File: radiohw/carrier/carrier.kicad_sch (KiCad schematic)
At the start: 4 parts, among them J2 Bus_M.2_Socket_B, J3 Bus_M.2_Socket_E, J5 USB_C_Receptacle, J6 USB3_A_Stacked

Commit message: Update schematics.
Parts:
- removed J2: Bus_M.2_Socket_B, symbol Connector:Bus_M.2_Socket_B
- added J4: Bus_M.2_Socket_M, symbol Connector:Bus_M.2_Socket_M
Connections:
- new net: J4.1 (GND), J4.15 (GND), J4.21 (GND), J4.27 (GND), J4.3 (GND), J4.33 (GND), J4.39 (GND), J4.45 (GND), J4.51 (GND), J4.57 (GND), J4.71 (GND), J4.73 (GND), J4.75 (GND), J4.9 (GND)
- new net: J4.12 (3.3V), J4.14 (3.3V), J4.16 (3.3V), J4.18 (3.3V), J4.2 (3.3V), J4.4 (3.3V), J4.70 (3.3V), J4.72 (3.3V), J4.74 (3.3V)
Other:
- added sheet 4GCard (4g_addon.kicad_sch)
- added sheet audio (audio.kicad_sch)
- moved on the sheet: J5, J6A, J6B
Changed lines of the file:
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@@
     (stroke (width 0) (type default))
   )
-  (symbol (lib_id "Connector:USB3_A_Stacked") (at 66.04 38.1 0) (unit 2)
-    (in_bom yes) (on_board yes) (dnp no) (fields_autoplaced)
-    (property "Reference" "J6" (at 66.04 19.05 0)
-      (effects (font (size 1.27 1.27)))
-    )
-    (property "Value" "USB3_A_Stacked" (at 66.04 21.59 0)
-      (effects (font (size 1.27 1.27)))
-    )
-    (property "Footprint" "" (at 69.85 35.56 0)
-      (effects (font (size 1.27 1.27)) hide)
-    )
-    (property "Datasheet" "~" (at 69.85 35.56 0)
+  (text_box "HDMI output\n\nAUDIO\n + 8 output channels minimum for main audio\n + 2 channel input for am/fm radio\n + 1 channel output for external radio\n + 1 channel input for external radio\n\nM2.B card for 4g addon\nM2.E card for wifi/bluetooth\nM2.M card for storage\n\nusb2\n + I touchscreen\n + I other stuff\n + E user charge only\n + E user charge only\n + E user charge only\n\nusb-c\n + user interface\n\nusb-3\n + user interface\n\ngpio\n + O winch in\n + O winch out\n + O4 window up\n + O4 window down\n + O door lock\n + O door unlock\n + O external radio trigger\n + O general led indicator\n + O fingerprint enable\n + O inverter enable\n + O4 light(s) control\n + O4 aux outputs\n + I potentiometer A for volume (quadrature)\n + I potentiometer B for volume (quadrature)\n + I potentiometer A for adjust (quadrature)\n + I potentiometer B for adjust (quadrature)\n + I button A\n + I button B\n + I fingerprint IRQ\n + I4 aux inputs\n\nuart\n + fingerprint sensor (3.3v)\n + GPS sensor\n\npcie\n + cameras add-on (on board)\n\n1G ethernet port\n\nNFC - ?\n\nam/fm radio control - ?\nam/fm radio data - ?\n\nsystem fan control and tachometer\n\nsim card connector ?"
+    (at 223.52 13.97 0) (size 55.88 149.86)
+    (stroke (width 0) (type default))
+    (fill (type none))
+    (effects (font (size 1.27 1.27)) (justify left top))
+  )
+  (symbol (lib_id "Connector:USB3_A_Stacked") (at 143.51 161.29 0) (unit 2)
+    (in_bom yes) (on_board yes) (dnp no) (fields_autoplaced)
+    (property "Reference" "J6" (at 143.51 142.24 0)
+      (effects (font (size 1.27 1.27)))
+    )
+    (property "Value" "USB3_A_Stacked" (at 143.51 144.78 0)
+      (effects (font (size 1.27 1.27)))
+    )
+    (property "Footprint" "" (at 147.32 158.75 0)
+      (effects (font (size 1.27 1.27)) hide)
+    )
+    (property "Datasheet" "~" (at 147.32 158.75 0)
       (effects (font (size 1.27 1.27)) hide)
     )
@@
     )
   )
-  (symbol (lib_id "Connector:Bus_M.2_Socket_B") (at 119.38 71.12 0) (unit 1)
-    (in_bom yes) (on_board yes) (dnp no) (fields_autoplaced)
-    (property "Reference" "J2" (at 121.5741 20.32 0)
-      (effects (font (size 1.27 1.27)) (justify left))
-    )
-    (property "Value" "Bus_M.2_Socket_B" (at 121.5741 22.86 0)
-      (effects (font (size 1.27 1.27)) (justify left))
-    )
-    (property "Footprint" "" (at 119.38 44.45 0)
-      (effects (font (size 1.27 1.27)) hide)
-    )
-    (property "Datasheet" "http://read.pudn.com/downloads794/doc/project/3133918/PCIe_M.2_Electromechanical_Spec_Rev1.0_Final_11012013_RS_Clean.pdf#page=154" (at 119.38 44.45 0)
-      (effects (font (size 1.27 1.27)) hide)
-    )
-    (pin "58")
-    (pin "4")
-    (pin "61")
-    (pin "44")
-    (pin "39")
-    (pin "59")
-    (pin "62")
-    (pin "60")
-    (pin "63")
-    (pin "25")
-    (pin "24")
-    (pin "26")
-    (pin "5")
-    (pin "11")
-    (pin "37")
-    (pin "30")
-    (pin "51")
-    (pin "2")
-    (pin "21")
-    (pin "65")
-    (pin "10")
-    (pin "74")
-    (pin "22")
-    (pin "42")
-    (pin "3")
-    (pin "64")
-    (pin "1")
-    (pin "9")
-    (pin "52")
-    (pin "70")
-    (pin "49")
-    (pin "38")
-    (pin "72")
-    (pin "71")
-    (pin "23")
-    (pin "31")
-    (pin "33")
-    (pin "35")
-    (pin "7")
-    (pin "54")
-    (pin "8")
-    (pin "41")
-    (pin "40")
-    (pin "27")
-    (pin "47")
-    (pin "66")
-    (pin "45")
-    (pin "20")
-    (pin "57")
-    (pin "48")
-    (pin "34")
-    (pin "69")
-    (pin "53")
-    (pin "55")
-    (pin "67")
-    (pin "68")
-    (pin "43")
-    (pin "75")
-    (pin "50")
-    (pin "6")
-    (pin "56")
-    (pin "29")
-    (pin "73")
-    (pin "46")
-    (pin "36")
-    (pin "32")
-    (pin "28")
-    (instances
-      (project "carrier"
-        (path "/041ef24b-cd87-4836-be30-e579ff56bff6"
-          (reference "J2") (unit 1)
-        )
-      )
-    )
-  )
-  (symbol (lib_id "Connector:USB3_A_Stacked") (at 33.02 40.64 0) (unit 1)
-    (in_bom yes) (on_board yes) (dnp no) (fields_autoplaced)
-    (property "Reference" "J6" (at 33.02 21.59 0)
-      (effects (font (size 1.27 1.27)))
-    )
-    (property "Value" "USB3_A_Stacked" (at 33.02 24.13 0)
-      (effects (font (size 1.27 1.27)))
-    )
-    (property "Footprint" "" (at 36.83 38.1 0)
-      (effects (font (size 1.27 1.27)) hide)
-    )
-    (property "Datasheet" "~" (at 36.83 38.1 0)
+  (symbol (lib_id "Connector:USB3_A_Stacked") (at 71.12 152.4 0) (unit 1)
+    (in_bom yes) (on_board yes) (dnp no) (fields_autoplaced)
+    (property "Reference" "J6" (at 71.12 133.35 0)
+      (effects (font (size 1.27 1.27)))
+    )
+    (property "Value" "USB3_A_Stacked" (at 71.12 135.89 0)
+      (effects (font (size 1.27 1.27)))
+    )
+    (property "Footprint" "" (at 74.93 149.86 0)
+      (effects (font (size 1.27 1.27)) hide)
+    )
+    (property "Datasheet" "~" (at 74.93 149.86 0)
       (effects (font (size 1.27 1.27)) hide)
     )
@@
         (path "/041ef24b-cd87-4836-be30-e579ff56bff6"
           (reference "J6") (unit 1)
+        )
+      )
+    )
+  )
+  (symbol (lib_id "Connector:Bus_M.2_Socket_M") (at 52.07 71.12 0) (unit 1)
+    (in_bom yes) (on_board yes) (dnp no) (fields_autoplaced)
+    (property "Reference" "J4" (at 54.2641 20.32 0)
+      (effects (font (size 1.27 1.27)) (justify left))
+    )
+    (property "Value" "Bus_M.2_Socket_M" (at 54.2641 22.86 0)
+      (effects (font (size 1.27 1.27)) (justify left))
+    )
+    (property "Footprint" "" (at 52.07 44.45 0)
+      (effects (font (size 1.27 1.27)) hide)
+    )
+    (property "Datasheet" "http://read.pudn.com/downloads794/doc/project/3133918/PCIe_M.2_Electromechanical_Spec_Rev1.0_Final_11012013_RS_Clean.pdf#page=155" (at 52.07 44.45 0)
+      (effects (font (size 1.27 1.27)) hide)
+    )
+    (pin "56")
+    (pin "28")
+    (pin "9")
+    (pin "70")
+    (pin "17")
+    (pin "54")
+    (pin "52")
+    (pin "41")
+    (pin "67")
+    (pin "25")
+    (pin "37")
+    (pin "58")
+    (pin "30")
+    (pin "27")
+    (pin "75")
+    (pin "14")
+    (pin "10")
+    (pin "33")
+    (pin "31")
+    (pin "24")
+    (pin "7")
+    (pin "8")
+    (pin "13")
+    (pin "38")
+    (pin "29")
+    (pin "6")
+    (pin "26")
+    (pin "45")
+    (pin "53")
+    (pin "69")
+    (pin "15")
+    (pin "22")
+    (pin "39")
+    (pin "42")
+    (pin "47")
+    (pin "18")
+    (pin "44")
+    (pin "57")
+    (pin "46")
+    (pin "43")
+    (pin "12")
+    (pin "32")
+    (pin "4")
+    (pin "11")
+    (pin "1")
+    (pin "71")
+    (pin "16")
+    (pin "20")
+    (pin "2")
+    (pin "23")
+    (pin "19")
+    (pin "21")
+    (pin "55")
+    (pin "68")
+    (pin "51")
+    (pin "73")
+    (pin "74")
+    (pin "35")
+    (pin "72")
+    (pin "50")
+    (pin "49")
+    (pin "34")
+    (pin "48")
+    (pin "5")
+    (pin "36")
+    (pin "40")
+    (pin "3")
+    (instances
+      (project "carrier"
+        (path "/041ef24b-cd87-4836-be30-e579ff56bff6"
+          (reference "J4") (unit 1)
         )
       )
@@
     )
   )
-  (symbol (lib_id "Connector:USB_C_Receptacle") (at 34.29 128.27 0) (unit 1)
-    (in_bom yes) (on_board yes) (dnp no) (fields_autoplaced)
-    (property "Reference" "J5" (at 34.29 95.25 0)
-      (effects (font (size 1.27 1.27)))
-    )
-    (property "Value" "USB_C_Receptacle" (at 34.29 97.79 0)
-      (effects (font (size 1.27 1.27)))
-    )
-    (property "Footprint" "" (at 38.1 128.27 0)
-      (effects (font (size 1.27 1.27)) hide)
-    )
-    (property "Datasheet" "https://www.usb.org/sites/default/files/documents/usb_type-c.zip" (at 38.1 128.27 0)
+  (symbol (lib_id "Connector:USB_C_Receptacle") (at 33.02 153.67 0) (unit 1)
+    (in_bom yes) (on_board yes) (dnp no) (fields_autoplaced)
+    (property "Reference" "J5" (at 33.02 120.65 0)
+      (effects (font (size 1.27 1.27)))
+    )
+    (property "Value" "USB_C_Receptacle" (at 33.02 123.19 0)
+      (effects (font (size 1.27 1.27)))
+    )
+    (property "Footprint" "" (at 36.83 153.67 0)
+      (effects (font (size 1.27 1.27)) hide)
+    )
+    (property "Datasheet" "https://www.usb.org/sites/default/files/documents/usb_type-c.zip" (at 36.83 153.67 0)
       (effects (font (size 1.27 1.27)) hide)
     )
@@
       )
     )
+  )
+  (sheet (at 176.53 121.92) (size 13.97 21.59) (fields_autoplaced)
+    (stroke (width 0.1524) (type solid))
+    (fill (color 0 0 0 0.0000))
+    (property "Sheetname" "audio" (at 176.53 121.2084 0)
+      (effects (font (size 1.27 1.27)) (justify left bottom))
+    )
+    (property "Sheetfile" "audio.kicad_sch" (at 176.53 144.0946 0)
+      (effects (font (size 1.27 1.27)) (justify left top))
+    )
+    (instances
+      (project "carrier"
+        (path "/041ef24b-cd87-4836-be30-e579ff56bff6" (page "3"))
+      )
+    )
+  )
+  (sheet (at 149.86 123.19) (size 12.7 10.16) (fields_autoplaced)
+    (stroke (width 0.1524) (type solid))
+    (fill (color 0 0 0 0.0000))
+    (property "Sheetname" "4GCard" (at 149.86 122.4784 0)
+      (effects (font (size 1.27 1.27)) (justify left bottom))
+    )
+    (property "Sheetfile" "4g_addon.kicad_sch" (at 149.86 133.9346 0)
+      (effects (font (size 1.27 1.27)) (justify left top))
+    )
+    (instances
+      (project "carrier"
+        (path "/041ef24b-cd87-4836-be30-e579ff56bff6" (page "4"))
+      )
+    )

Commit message: Schematic development.
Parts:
- removed J3: Bus_M.2_Socket_E, symbol Connector:Bus_M.2_Socket_E
- removed J4: Bus_M.2_Socket_M, symbol Connector:Bus_M.2_Socket_M
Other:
- added sheet GPIO (gpio.kicad_sch)
- added sheet storage (storage.kicad_sch)
- added sheet wireless (wireless.kicad_sch)
- sheet ComExpressCarrier ports: added none; removed GBE0_MDI3+, GBE0_MDI3-
- note added: "TODO usb for wireless"
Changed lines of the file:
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@@
     (effects (font (size 1.27 1.27)) (justify left top))
+  )
+  (text "TODO\nusb for wireless" (at 88.9 25.4 0)
+    (effects (font (size 1.27 1.27)) (justify left bottom))
   )
   (symbol (lib_id "Connector:USB3_A_Stacked") (at 143.51 161.29 0) (unit 2)
@@
         (path "/041ef24b-cd87-4836-be30-e579ff56bff6"
           (reference "J6") (unit 1)
-        )
-      )
-    )
-  )
-  (symbol (lib_id "Connector:Bus_M.2_Socket_M") (at 52.07 71.12 0) (unit 1)
-    (in_bom yes) (on_board yes) (dnp no) (fields_autoplaced)
-    (property "Reference" "J4" (at 54.2641 20.32 0)
-      (effects (font (size 1.27 1.27)) (justify left))
-    )
-    (property "Value" "Bus_M.2_Socket_M" (at 54.2641 22.86 0)
-      (effects (font (size 1.27 1.27)) (justify left))
-    )
-    (property "Footprint" "" (at 52.07 44.45 0)
-      (effects (font (size 1.27 1.27)) hide)
-    )
-    (property "Datasheet" "http://read.pudn.com/downloads794/doc/project/3133918/PCIe_M.2_Electromechanical_Spec_Rev1.0_Final_11012013_RS_Clean.pdf#page=155" (at 52.07 44.45 0)
-      (effects (font (size 1.27 1.27)) hide)
-    )
-    (pin "56")
-    (pin "28")
-    (pin "9")
-    (pin "70")
-    (pin "17")
-    (pin "54")
-    (pin "52")
-    (pin "41")
-    (pin "67")
-    (pin "25")
-    (pin "37")
-    (pin "58")
-    (pin "30")
-    (pin "27")
-    (pin "75")
-    (pin "14")
-    (pin "10")
-    (pin "33")
-    (pin "31")
-    (pin "24")
-    (pin "7")
-    (pin "8")
-    (pin "13")
-    (pin "38")
-    (pin "29")
-    (pin "6")
-    (pin "26")
-    (pin "45")
-    (pin "53")
-    (pin "69")
-    (pin "15")
-    (pin "22")
-    (pin "39")
-    (pin "42")
-    (pin "47")
-    (pin "18")
-    (pin "44")
-    (pin "57")
-    (pin "46")
-    (pin "43")
-    (pin "12")
-    (pin "32")
-    (pin "4")
-    (pin "11")
-    (pin "1")
-    (pin "71")
-    (pin "16")
-    (pin "20")
-    (pin "2")
-    (pin "23")
-    (pin "19")
-    (pin "21")
-    (pin "55")
-    (pin "68")
-    (pin "51")
-    (pin "73")
-    (pin "74")
-    (pin "35")
-    (pin "72")
-    (pin "50")
-    (pin "49")
-    (pin "34")
-    (pin "48")
-    (pin "5")
-    (pin "36")
-    (pin "40")
-    (pin "3")
-    (instances
-      (project "carrier"
-        (path "/041ef24b-cd87-4836-be30-e579ff56bff6"
-          (reference "J4") (unit 1)
-        )
-      )
-    )
-  )
-  (symbol (lib_id "Connector:Bus_M.2_Socket_E") (at 191.77 71.12 0) (unit 1)
-    (in_bom yes) (on_board yes) (dnp no) (fields_autoplaced)
-    (property "Reference" "J3" (at 193.9641 20.32 0)
-      (effects (font (size 1.27 1.27)) (justify left))
-    )
-    (property "Value" "Bus_M.2_Socket_E" (at 193.9641 22.86 0)
-      (effects (font (size 1.27 1.27)) (justify left))
-    )
-    (property "Footprint" "" (at 191.77 44.45 0)
-      (effects (font (size 1.27 1.27)) hide)
-    )
-    (property "Datasheet" "http://read.pudn.com/downloads794/doc/project/3133918/PCIe_M.2_Electromechanical_Spec_Rev1.0_Final_11012013_RS_Clean.pdf#page=150" (at 191.77 44.45 0)
-      (effects (font (size 1.27 1.27)) hide)
-    )
-    (pin "32")
-    (pin "22")
-    (pin "33")
-    (pin "69")
-    (pin "12")
-    (pin "37")
-    (pin "48")
-    (pin "35")
-    (pin "1")
-    (pin "47")
-    (pin "11")
-    (pin "55")
-    (pin "36")
-    (pin "13")
-    (pin "57")
-    (pin "34")
-    (pin "38")
-    (pin "59")
-    (pin "66")
-    (pin "19")
-    (pin "10")
-    (pin "8")
-    (pin "41")
-    (pin "23")
-    (pin "18")
-    (pin "17")
-    (pin "58")
-    (pin "14")
-    (pin "15")
-    (pin "44")
-    (pin "45")
-    (pin "7")
-    (pin "70")
-    (pin "56")
-    (pin "46")
-    (pin "67")
-    (pin "2")
-    (pin "73")
-    (pin "63")
-    (pin "68")
-    (pin "4")
-    (pin "3")
-    (pin "40")
-    (pin "20")
-    (pin "43")
-    (pin "52")
-    (pin "42")
-    (pin "64")
-    (pin "65")
-    (pin "54")
-    (pin "5")
-    (pin "71")
-    (pin "39")
-    (pin "51")
-    (pin "61")
-    (pin "72")
-    (pin "74")
-    (pin "16")
-    (pin "21")
-    (pin "60")
-    (pin "53")
-    (pin "6")
-    (pin "75")
-    (pin "49")
-    (pin "9")
-    (pin "62")
-    (pin "50")
-    (instances
-      (project "carrier"
-        (path "/041ef24b-cd87-4836-be30-e579ff56bff6"
-          (reference "J3") (unit 1)
         )
       )
@@
       (effects (font (size 1.27 1.27)) (justify left top))
     )
-    (pin "GBE0_MDI3-" input (at 88.9 166.37 180)
-      (effects (font (size 1.27 1.27)) (justify left))
-    )
-    (pin "GBE0_MDI3+" input (at 88.9 168.91 180)
-      (effects (font (size 1.27 1.27)) (justify left))
-    )
     (instances
       (project "carrier"
@@
       )
     )
+  )
+  (sheet (at 147.32 92.71) (size 12.7 3.81) (fields_autoplaced)
+    (stroke (width 0.1524) (type solid))
+    (fill (color 0 0 0 0.0000))
+    (property "Sheetname" "storage" (at 147.32 91.9984 0)
+      (effects (font (size 1.27 1.27)) (justify left bottom))
+    )
+    (property "Sheetfile" "storage.kicad_sch" (at 147.32 97.1046 0)
+      (effects (font (size 1.27 1.27)) (justify left top))
+    )
+    (instances
+      (project "carrier"
+        (path "/041ef24b-cd87-4836-be30-e579ff56bff6" (page "7"))
+      )
+    )
+  )
+  (sheet (at 146.05 74.93) (size 12.7 7.62) (fields_autoplaced)
+    (stroke (width 0.1524) (type solid))
+    (fill (color 0 0 0 0.0000))
+    (property "Sheetname" "wireless" (at 146.05 74.2184 0)
+      (effects (font (size 1.27 1.27)) (justify left bottom))
+    )
+    (property "Sheetfile" "wireless.kicad_sch" (at 146.05 83.1346 0)
+      (effects (font (size 1.27 1.27)) (justify left top))
+    )
+    (instances
+      (project "carrier"
+        (path "/041ef24b-cd87-4836-be30-e579ff56bff6" (page "6"))
+      )
+    )
+  )
+  (sheet (at 198.12 124.46) (size 12.7 3.81) (fields_autoplaced)
+    (stroke (width 0.1524) (type solid))
+    (fill (color 0 0 0 0.0000))
+    (property "Sheetname" "GPIO" (at 198.12 123.7484 0)
+      (effects (font (size 1.27 1.27)) (justify left bottom))
+    )
+    (property "Sheetfile" "gpio.kicad_sch" (at 198.12 128.8546 0)
+      (effects (font (size 1.27 1.27)) (justify left top))
+    )
+    (instances
+      (project "carrier"
+        (path "/041ef24b-cd87-4836-be30-e579ff56bff6" (page "6"))
+      )
+    )

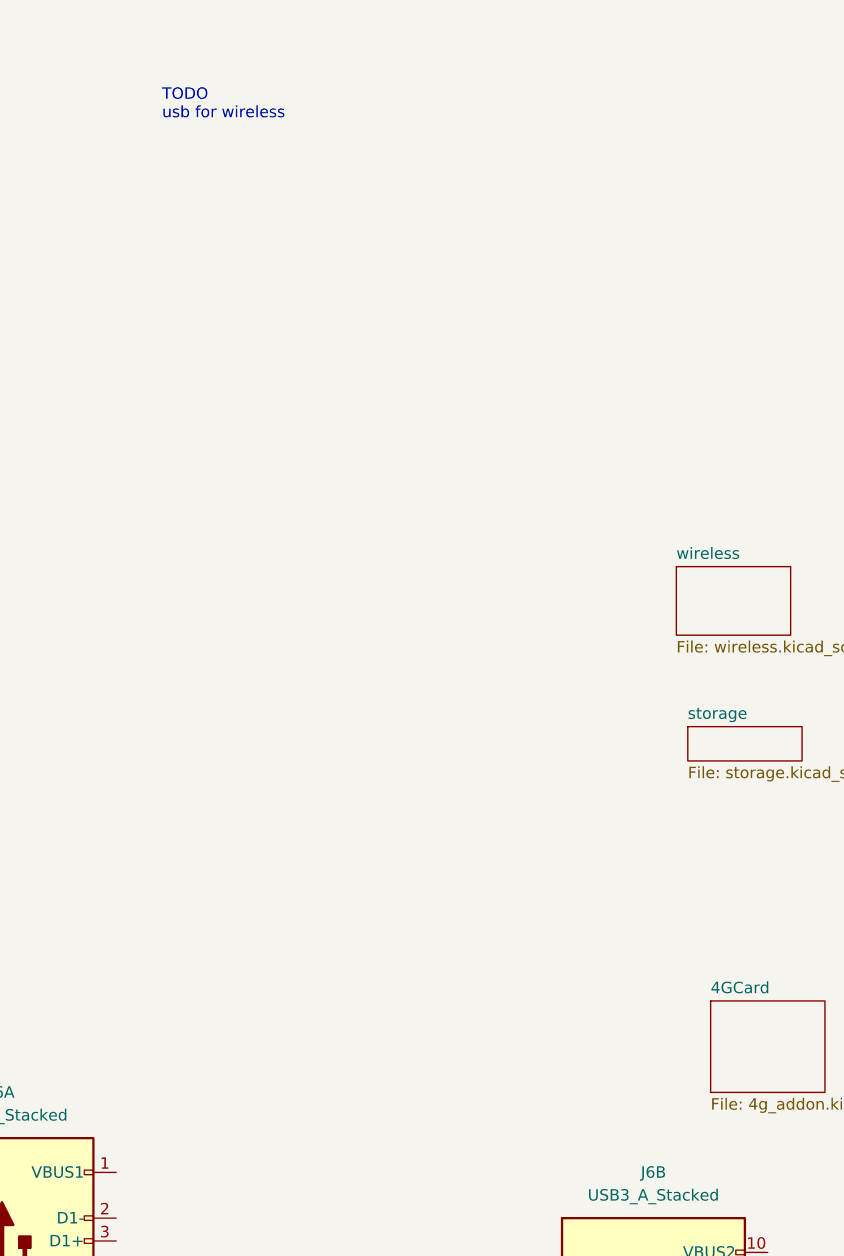
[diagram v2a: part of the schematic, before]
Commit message: Add accelerometer and i2c bus isolator to schematic.
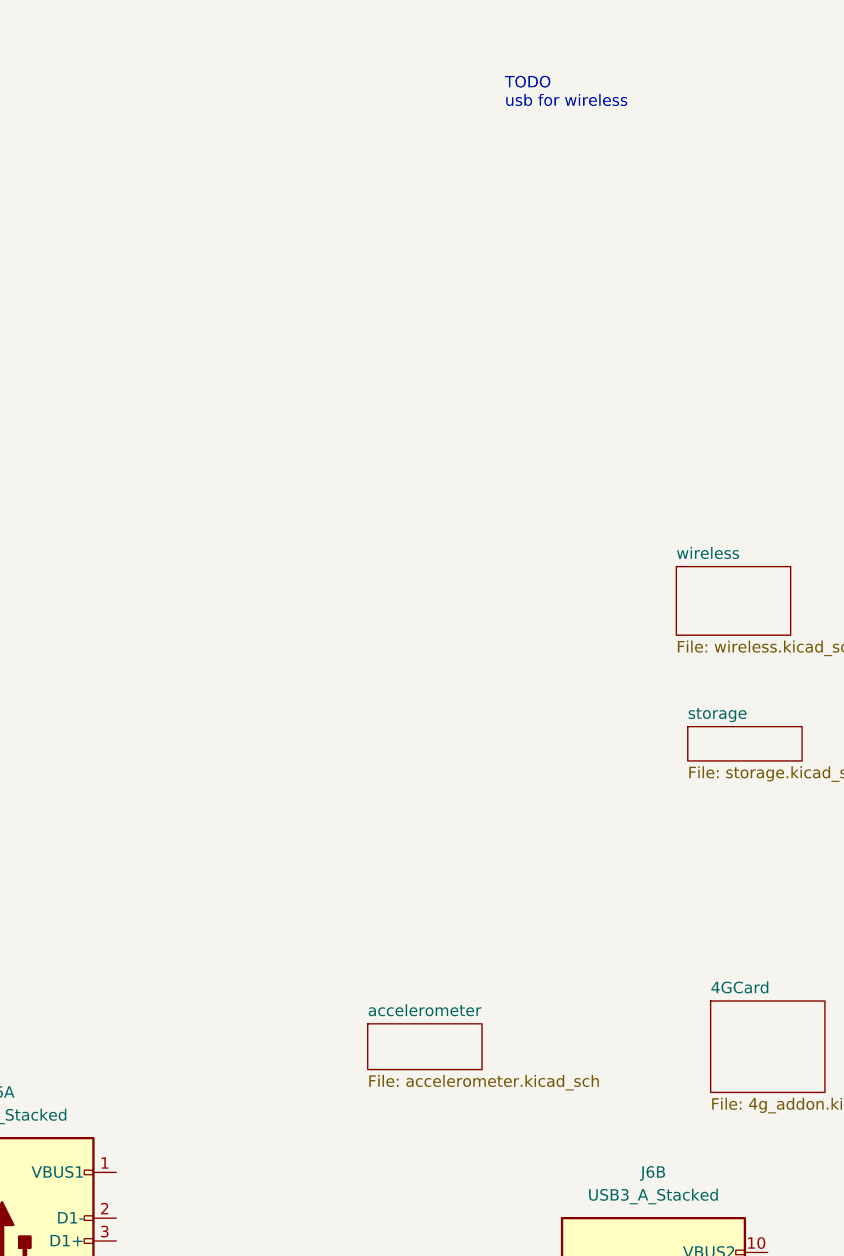
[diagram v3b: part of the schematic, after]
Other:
- added sheet accelerometer (accelerometer.kicad_sch)
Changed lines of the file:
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@@
     (effects (font (size 1.27 1.27)) (justify left top))
   )
-  (text "TODO\nusb for wireless" (at 88.9 25.4 0)
+  (text "TODO\nusb for wireless" (at 127 24.13 0)
     (effects (font (size 1.27 1.27)) (justify left bottom))
   )
@@
       )
     )
+  )
+  (sheet (at 111.76 125.73) (size 12.7 5.08) (fields_autoplaced)
+    (stroke (width 0.1524) (type solid))
+    (fill (color 0 0 0 0.0000))
+    (property "Sheetname" "accelerometer" (at 111.76 125.0184 0)
+      (effects (font (size 1.27 1.27)) (justify left bottom))
+    )
+    (property "Sheetfile" "accelerometer.kicad_sch" (at 111.76 131.3946 0)
+      (effects (font (size 1.27 1.27)) (justify left top))
+    )
+    (instances
+      (project "carrier"
+        (path "/041ef24b-cd87-4836-be30-e579ff56bff6" (page "11"))
+      )
+    )
